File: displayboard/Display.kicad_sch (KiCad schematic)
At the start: 15 parts, among them Q1401 NPN, X1401 Touch, X1402 Display, X1403 External

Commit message: Remove old production files, add cutout for the programming cable, add connector for mainboard cable
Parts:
- removed R1401, R1402, R1403, R1408, R1411: 10k, Resistor_SMD:R_0805_2012Metric, symbol Device:R
- removed R1409, R1410: 3k3, Resistor_SMD:R_0805_2012Metric, symbol Device:R
- removed X1403: External, Connector_PinHeader_2.54mm:PinHeader_1x14_P2.54mm_Vertical, symbol Connector_Generic:Conn_01x14
- added X503: Mainboard, Connector_FFC-FPC:Amphenol_F32R-1A7x1-11014_1x14-1MP_P0.5mm_Horizontal, symbol Connector_Generic_MountingPin:Conn_01x14_MountingPin
- renumbered Q1401 to Q501, R1407 to R501, R1404 to R502, R1405 to R503, R1406 to R504, X1401 to X501, X1402 to X502
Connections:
- net +3V3: now also X503.1 (Pin_1)
- net Display-Backlight: now also X503.14 (Pin_14)
- net Display-DC: now also X503.10 (Pin_10)
- net GND: now also X503.2 (Pin_2), X503.MP (MountPin)
- net I2C-SCL: now also X503.6 (Pin_6)
- net I2C-SDA: now also X503.5 (Pin_5)
- net SPI-MISO: now also X503.13 (Pin_13)
- net SPI-MOSI: now also X503.12 (Pin_12)
- net SPI-SCLK: now also X503.9 (Pin_9)
- net ~{Display-CS}: now also X503.11 (Pin_11)
- net ~{Display-Reset}: now also X503.8 (Pin_8)
- net ~{Touch-IRQ}: now also X503.4 (Pin_4)
- net ~{Touch-Reset}: now also X503.3 (Pin_3)
- new net ~{Expander-Int}: X503.7 (Pin_7)

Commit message: Prepare Release 1.0.0
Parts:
- X501: symbol Connector_Generic:Conn_01x06 -> Connector_Generic_MountingPin:Conn_01x06_MountingPin
- X502: footprint Connector_FFC-FPC:TE_1-84952-8_1x18-1MP_P1.0mm_Horizontal -> Molex_Kampi:5051101892; symbol Connector_Generic:Conn_01x18 -> Connector_Generic_MountingPin:Conn_01x18_MountingPin; manf (none) -> Molex; manf# (none) -> 505110-1892; mouser# (none) -> 538-505110-1892
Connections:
- net GND: now also X501.MP (MountPin), X502.MP (MountPin)

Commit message: Changed: Add missing part informations
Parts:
- R502: manf (none) -> Bourns; manf# (none) -> CRS0805-JX-100ELF; mouser# (none) -> 652-CRS0805-JX-100ELF
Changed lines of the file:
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@@
 			)
 		)
-		(property "Datasheet" "~"
+		(property "Datasheet" "https://www.molex.com/en-us/products/part-detail-pdf/5051101892?display=pdf"
 			(at 55.88 118.11 0)
 			(effects
@@
 			)
 		)
-		(property "Datasheet" "~"
+		(property "Datasheet" "https://cdn.amphenol-cs.com/media/wysiwyg/files/drawing/f32r-f32j.pdf"
 			(at 55.88 57.15 0)
 			(effects
@@
 			)
 		)
-		(property "Datasheet" ""
+		(property "Datasheet" "https://www.mouser.de/datasheet/3/40/1/CRS.pdf"
 			(at 85.09 123.19 0)
 			(effects
@@
 			)
 		)
-		(property "manf" ""
+		(property "manf" "Bourns"
 			(at 85.09 123.19 0)
 			(effects
@@
 			)
 		)
-		(property "manf#" ""
+		(property "manf#" "CRS0805-JX-100ELF"
 			(at 85.09 123.19 0)
 			(effects
@@
 			)
 		)
-		(property "mouser#" ""
+		(property "mouser#" "652-CRS0805-JX-100ELF"
 			(at 85.09 123.19 0)
 			(effects

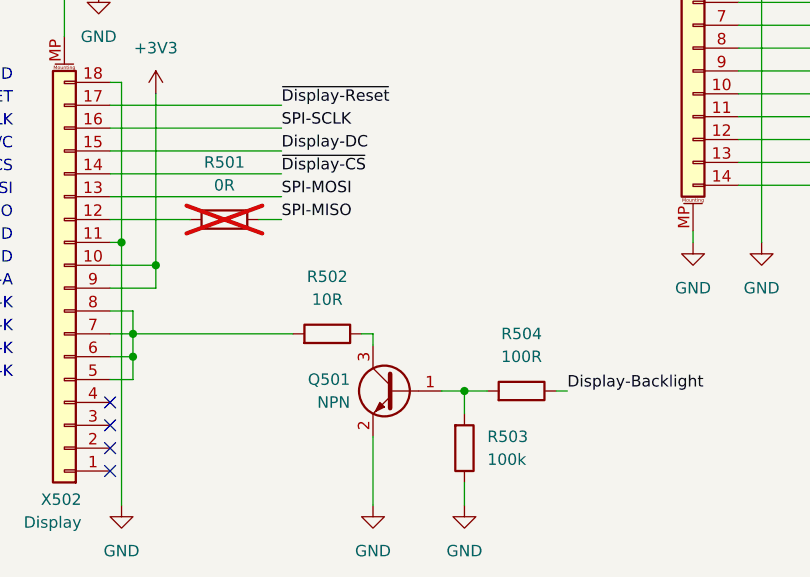
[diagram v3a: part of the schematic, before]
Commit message: Added: Add a cutout for the display cable, add different assembly improvements
Signed-off-by: Daniel Kampert <DanielKampert@kampis-elektroecke.de>
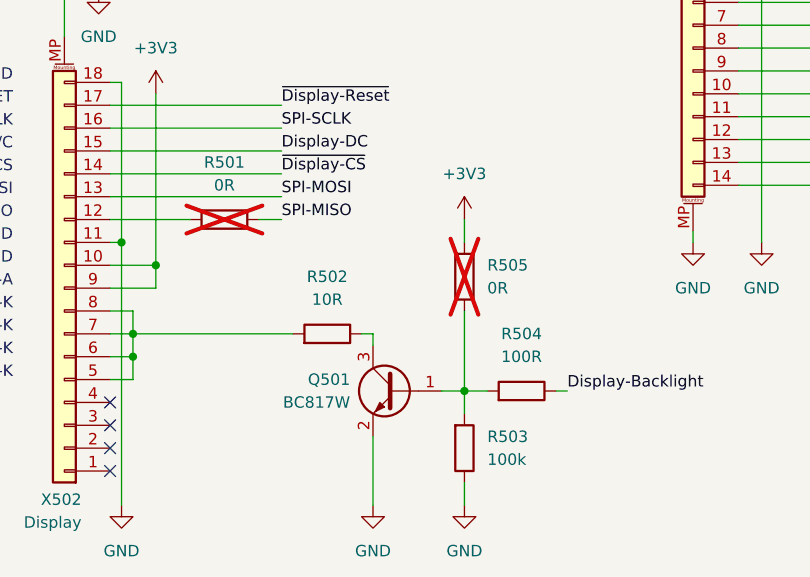
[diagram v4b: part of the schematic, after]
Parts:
- added R505: 0R, Resistor_SMD:R_0805_2012Metric, symbol Device:R
- Q501: value NPN -> BC817W
- X502: manf Molex -> Amphenol Aorora; manf# 505110-1892 -> F32R-1A7H1-11018; mouser# 538-505110-1892 -> 649-F32R-1A7H1-11018
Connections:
- net +3V3: now also R505.1
- net at Q501.1 (B), R503.2, R504.2: now also R505.2
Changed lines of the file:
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@@
+	(wire
+		(pts
+			(xy 100.33 120.65) (xy 100.33 129.54)
+		)
+		(stroke
+			(width 0)
+			(type default)
+		)
+	)
 	(wire
 		(pts
@@
 		(pts
 			(xy 60.96 59.69) (xy 80.01 59.69)
+		)
+		(stroke
+			(width 0)
+			(type default)
+		)
+	)
+	(wire
+		(pts
+			(xy 100.33 110.49) (xy 100.33 113.03)
 		)
 		(stroke
@@
 				(path "/d5742f03-3b1a-42e5-a384-018bd4b919aa/c5103ceb-5325-4a84-a025-9638a412984e/87ec52b1-2e4e-4bae-bd8b-72c5c03421b9"
 					(reference "#PWR0502")
+					(unit 1)
+				)
+			)
+		)
+	)
+	(symbol
+		(lib_id "Device:R")
+		(at 100.33 116.84 0)
+		(mirror y)
+		(unit 1)
+		(exclude_from_sim no)
+		(in_bom no)
+		(on_board yes)
+		(dnp yes)
+		(fields_autoplaced yes)
+		(property "Reference" "R505"
+			(at 102.87 115.5699 0)
+			(effects
+				(font
+					(size 1.27 1.27)
+				)
+				(justify right)
+			)
+		)
+		(property "Value" "0R"
+			(at 102.87 118.1099 0)
+			(effects
+				(font
+					(size 1.27 1.27)
+				)
+				(justify right)
+			)
+		)
+		(property "Footprint" "Resistor_SMD:R_0805_2012Metric"
+			(at 102.108 116.84 90)
+			(effects
+				(font
+					(size 1.27 1.27)
+				)
+				(hide yes)
+			)
+		)
+		(property "Datasheet" ""
+			(at 100.33 116.84 0)
+			(effects
+				(font
+					(size 1.27 1.27)
+				)
+				(hide yes)
+			)
+		)
+		(property "Description" "Resistor"
+			(at 100.33 116.84 0)
+			(effects
+				(font
+					(size 1.27 1.27)
+				)
+				(hide yes)
+			)
+		)
+		(property "CONFIG" ""
+			(at 100.33 116.84 0)
+			(effects
+				(font
+					(size 1.27 1.27)
+				)
+				(hide yes)
+			)
+		)
+		(property "manf" ""
+			(at 100.33 116.84 0)
+			(effects
+				(font
+					(size 1.27 1.27)
+				)
+				(hide yes)
+			)
+		)
+		(property "manf#" ""
+			(at 100.33 116.84 0)
+			(effects
+				(font
+					(size 1.27 1.27)
+				)
+				(hide yes)
+			)
+		)
+		(property "mouser#" ""
+			(at 100.33 116.84 0)
+			(effects
+				(font
+					(size 1.27 1.27)
+				)
+				(hide yes)
+			)
+		)
+		(pin "1"
+		)
+		(pin "2"
+		)
+		(instances
+			(project "Displayboard"
+				(path "/d5742f03-3b1a-42e5-a384-018bd4b919aa/c5103ceb-5325-4a84-a025-9638a412984e/87ec52b1-2e4e-4bae-bd8b-72c5c03421b9"
+					(reference "R505")
 					(unit 1)
 				)
@@
 			)
 		)
-		(property "Value" "NPN"
+		(property "Value" "BC817W"
 			(at 87.63 130.8099 0)
 			(effects
@@
 			)
 		)
-		(property "Datasheet" "https://www.molex.com/en-us/products/part-detail-pdf/5051101892?display=pdf"
+		(property "Datasheet" "https://cdn.amphenol-cs.com/media/wysiwyg/files/drawing/f32r-f32j.pdf"
 			(at 55.88 118.11 0)
 			(effects
@@
 			)
 		)
-		(property "manf" "Molex"
+		(property "manf" "Amphenol Aorora"
 			(at 55.88 118.11 0)
 			(effects
@@
 			)
 		)
-		(property "manf#" "505110-1892"
+		(property "manf#" "F32R-1A7H1-11018"
 			(at 55.88 118.11 0)
 			(effects
@@
 			)
 		)
-		(property "mouser#" "538-505110-1892"
+		(property "mouser#" "649-F32R-1A7H1-11018"
 			(at 55.88 118.11 0)
 			(effects
@@
 					(unit 1)
 				)
+			)
+		)
+	)
+	(symbol
+		(lib_id "power:+3V3")
+		(at 100.33 110.49 0)
+		(unit 1)
+		(exclude_from_sim no)
+		(in_bom yes)
+		(on_board yes)
+		(dnp no)
+		(fields_autoplaced yes)
+		(property "Reference" "#PWR0514"
+			(at 100.33 114.3 0)
+			(effects
+				(font
+					(size 1.27 1.27)
+				)
+				(hide yes)
+			)
+		)
+		(property "Value" "+3V3"
+			(at 100.33 105.41 0)
+			(effects
+				(font
+					(size 1.27 1.27)
+				)
+			)
+		)
+		(property "Footprint" ""
+			(at 100.33 110.49 0)
+			(effects
+				(font
+					(size 1.27 1.27)
+				)
+				(hide yes)
+			)
+		)
+		(property "Datasheet" ""
+			(at 100.33 110.49 0)
+			(effects
+				(font
+					(size 1.27 1.27)
+				)
+				(hide yes)
+			)
+		)
+		(property "Description" "Power symbol creates a global label with name \"+3V3\""
+			(at 100.33 110.49 0)
+			(effects
+				(font
+					(size 1.27 1.27)
+				)
+				(hide yes)
+			)
+		)
+		(pin "1"
+		)
+		(instances
+			(project "Displayboard"
+				(path "/d5742f03-3b1a-42e5-a384-018bd4b919aa/c5103ceb-5325-4a84-a025-9638a412984e/87ec52b1-2e4e-4bae-bd8b-72c5c03421b9"
+					(reference "#PWR0514")
+					(unit 1)
+				)

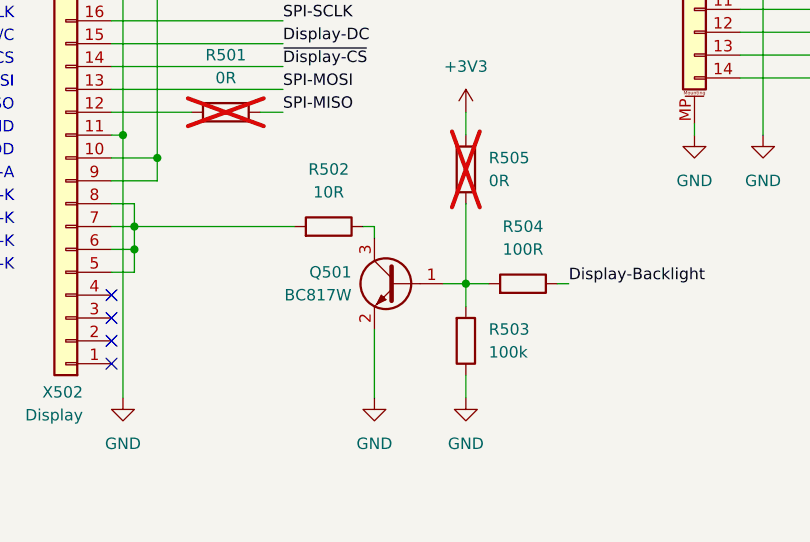
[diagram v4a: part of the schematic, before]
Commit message: Feature: Add debounce capacitors to push buttons
- Replace NPN transistor with N-Channel MOSFET

Signed-off-by: Daniel Kampert <DanielKampert@kampis-elektroecke.de>
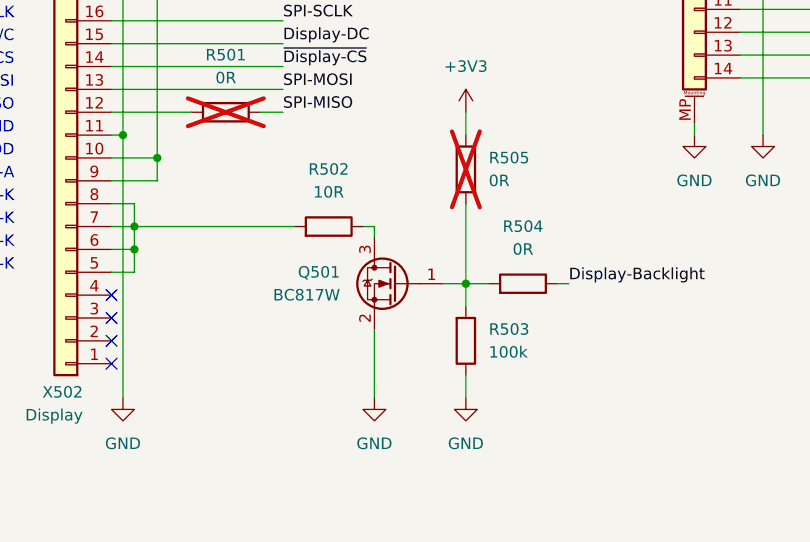
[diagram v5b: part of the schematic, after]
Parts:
- Q501: symbol Transistor_BJT:BC817 -> Nexperia:PMV50XNEAR
- R504: value 100R -> 0R; manf# CR0805-JW-101ELF -> CR0805AJ/-000EAS; mouser# 652-CR0805-JW-101ELF -> 652-CR0805AJ/-000EAS
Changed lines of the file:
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@@
 	)
 	(symbol
-		(lib_id "Transistor_BJT:BC817")
-		(at 92.71 129.54 0)
+		(lib_id "Nexperia:PMV50XNEAR")
+		(at 90.17 129.54 0)
 		(mirror y)
 		(unit 1)
@@
 		(fields_autoplaced yes)
 		(property "Reference" "Q501"
-			(at 87.63 128.2699 0)
+			(at 86.36 128.2699 0)
 			(effects
 				(font
@@
 		)
 		(property "Value" "BC817W"
-			(at 87.63 130.8099 0)
+			(at 86.36 130.8099 0)
 			(effects
 				(font
@@
 		)
 		(property "Footprint" "Package_TO_SOT_SMD:SOT-23"
-			(at 87.63 131.445 0)
-			(effects
-				(font
-					(size 1.27 1.27)
-					(italic yes)
-				)
-				(justify left)
-				(hide yes)
-			)
-		)
-		(property "Datasheet" "https://assets.nexperia.com/documents/data-sheet/BC817W_SER.pdf"
-			(at 92.71 129.54 0)
-			(effects
-				(font
-					(size 1.27 1.27)
-				)
-				(justify left)
-				(hide yes)
-			)
-		)
-		(property "Description" "0.8A Ic, 45V Vce, NPN Transistor, SOT-23"
-			(at 92.71 129.54 0)
+			(at 90.17 129.54 0)
+			(effects
+				(font
+					(size 1.27 1.27)
+				)
+				(hide yes)
+			)
+		)
+		(property "Datasheet" "https://assets.nexperia.com/documents/data-sheet/PMV50XNEA.pdf"
+			(at 90.17 129.54 0)
+			(effects
+				(font
+					(size 1.27 1.27)
+				)
+				(hide yes)
+			)
+		)
+		(property "Description" "3.4A Id, 30V Vds, N-Channel MOSFET, SOT-23"
+			(at 90.17 129.54 0)
 			(effects
 				(font
@@
 		)
 		(property "manf" "Nexperia"
-			(at 92.71 129.54 0)
+			(at 90.17 129.54 0)
 			(effects
 				(font
@@
 		)
 		(property "manf#" "BC817W,135"
-			(at 92.71 129.54 0)
+			(at 90.17 129.54 0)
 			(effects
 				(font
@@
 		)
 		(property "mouser#" "771-BC817W,135"
-			(at 92.71 129.54 0)
+			(at 90.17 129.54 0)
 			(effects
 				(font
@@
 		)
 		(property "CONFIG" ""
-			(at 92.71 129.54 0)
+			(at 90.17 129.54 0)
 			(effects
 				(font
@@
 			)
 		)
-		(property "Value" "100R"
+		(property "Value" "0R"
 			(at 106.68 125.73 90)
 			(effects
@@
 			)
 		)
-		(property "Datasheet" "https://eu.mouser.com/datasheet/3/40/1/cr.pdf"
+		(property "Datasheet" "https://www.mouser.de/datasheet/3/40/1/cr_a_as.pdf"
 			(at 106.68 129.54 0)
 			(effects
@@
 			)
 		)
-		(property "manf#" "CR0805-JW-101ELF"
+		(property "manf#" "CR0805AJ/-000EAS"
 			(at 106.68 129.54 0)
 			(effects
@@
 			)
 		)
-		(property "mouser#" "652-CR0805-JW-101ELF"
+		(property "mouser#" "652-CR0805AJ/-000EAS"
 			(at 106.68 129.54 0)
 			(effects
